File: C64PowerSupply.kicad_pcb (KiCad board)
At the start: 2 copper layers, 127 x 76.2 mm, 32 parts, among them J1 120V IN, J2 OUT C64, J3 OUT C128, SW1 120/240V SELECT, U1 BD9E303EFJ-LBE2

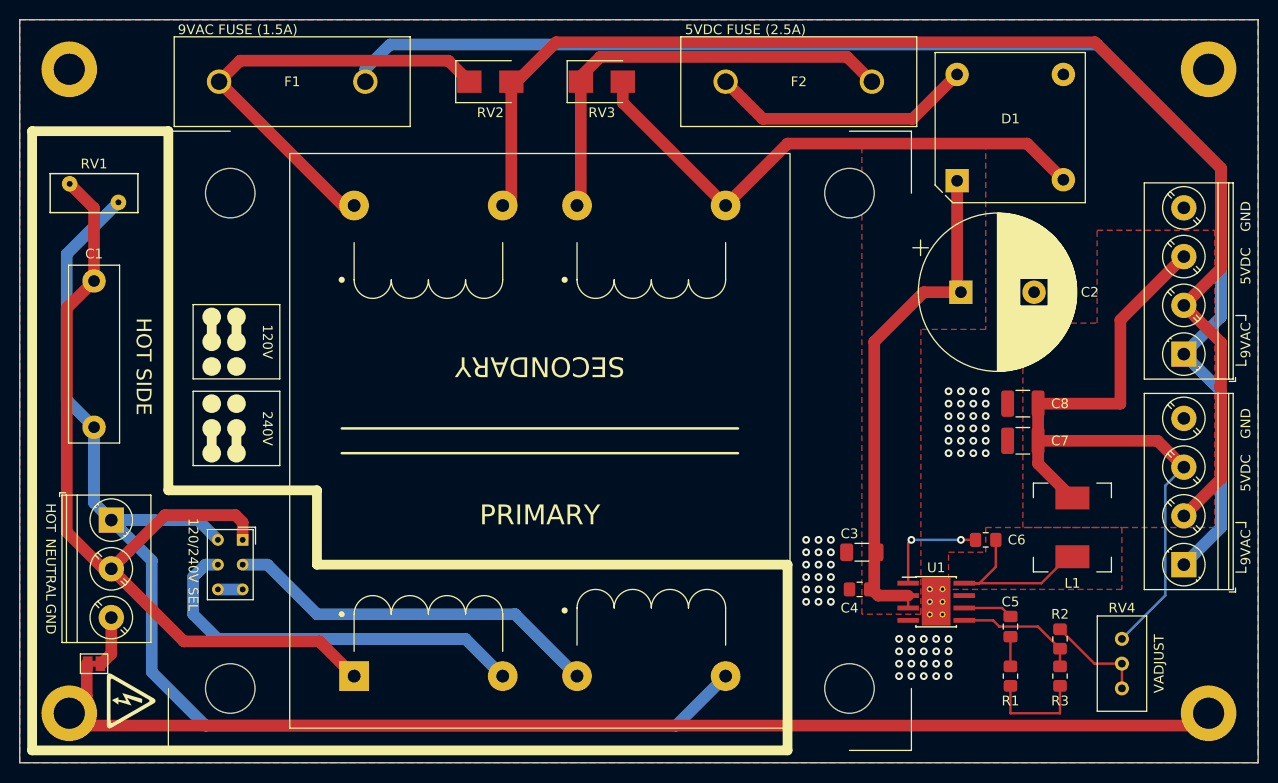
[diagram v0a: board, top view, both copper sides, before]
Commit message: Transformer hole size
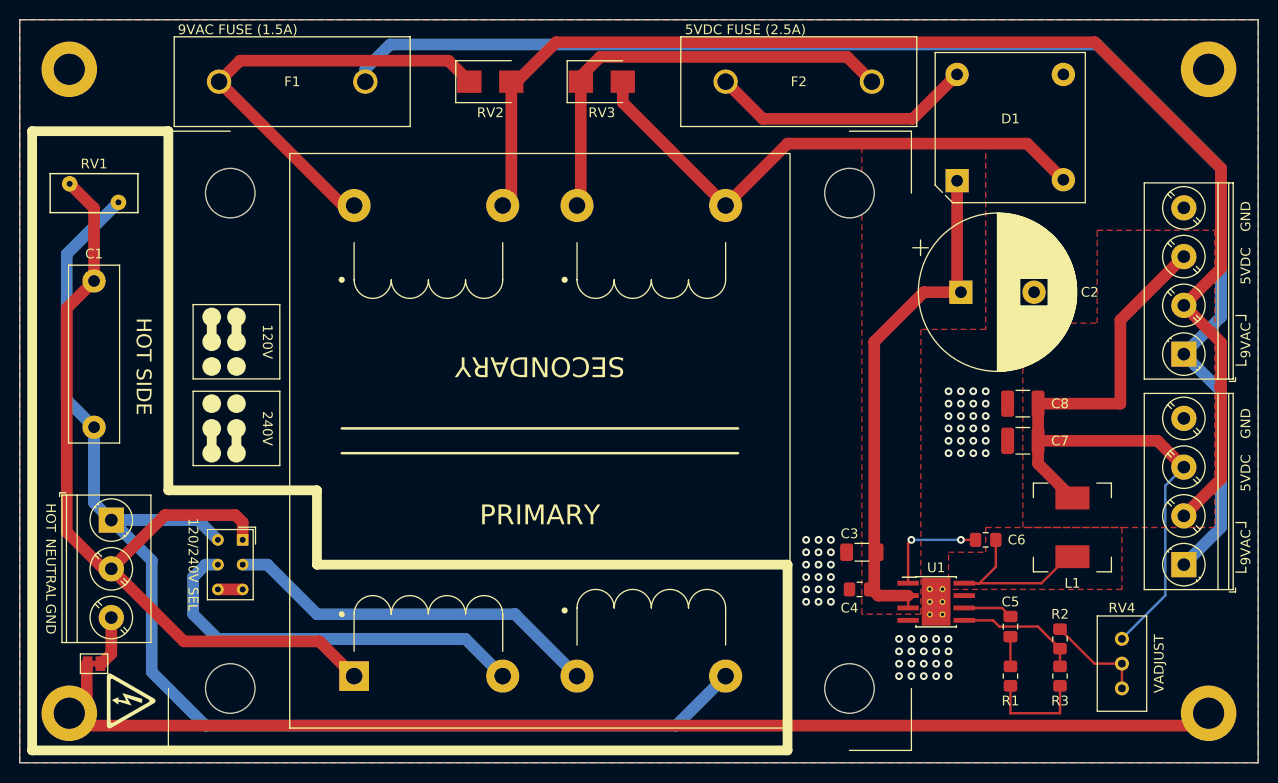
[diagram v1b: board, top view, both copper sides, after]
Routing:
- net GND: track 134.4 -> 130.8 mm

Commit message: Voltage sel switch footprint
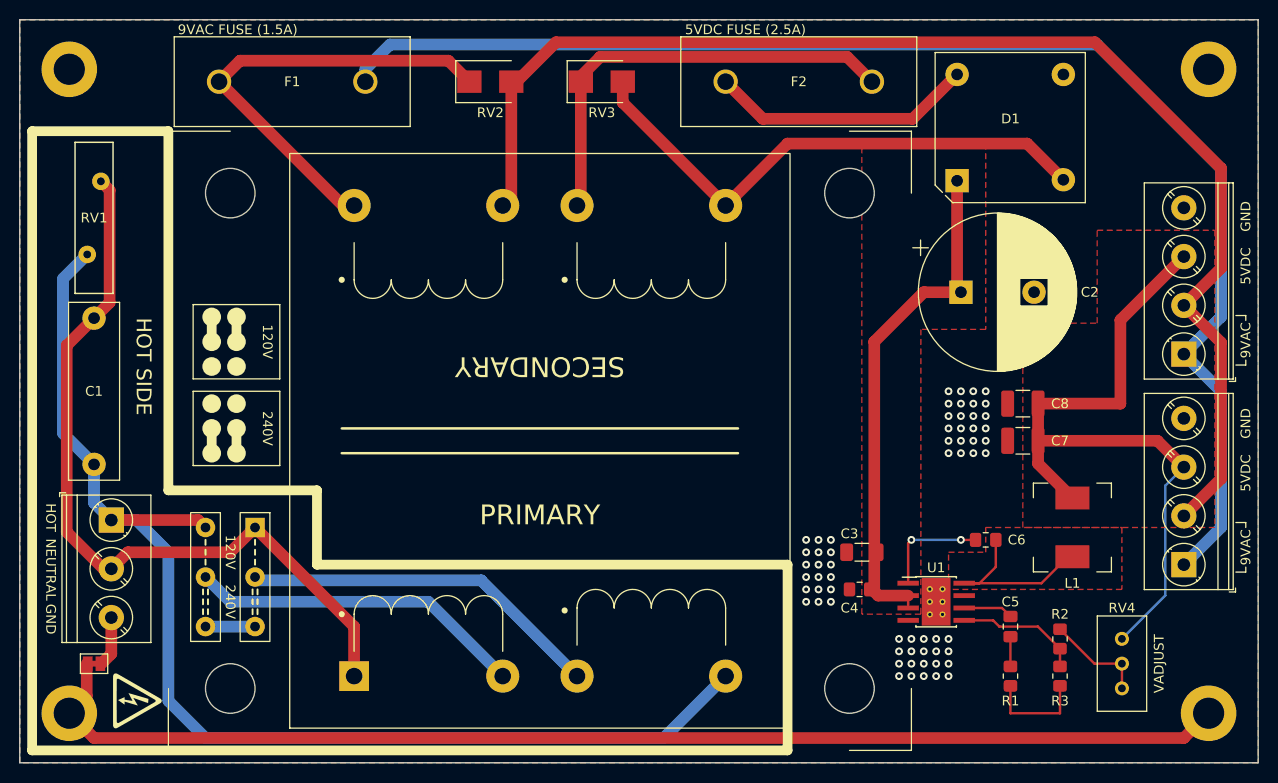
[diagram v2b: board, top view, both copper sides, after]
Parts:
- RV1: footprint Varistor:RV_Disc_D9mm_W4mm_P5mm -> Varistor:RV_Disc_D15.5mm_W3.9mm_P7.5mm
- SW1: footprint Button_Switch_THT:SW_NKK_GW12LJP -> DTLib:V_SEL_SWITCH
- moved G*** 10.2 mm to (142.2, 111.8)
- moved RV1 6.23 mm to (75.5, 74.9), turned to 90 degrees
- moved C1 3.81 mm to (76.2, 96.4)
- moved SW1 1.80 mm to (92.7, 102.9)
- moved G*** 0.63 mm to (80.6, 120.7)
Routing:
- net AC_NEUTRAL: track 91.4 -> 80.2 mm
- net Net-(SW1-Pad5): track 41.3 -> 34.7 mm
- net AC_HOT: track 129.0 -> 124.1 mm
- net Net-(SW1-Pad3): track 2.54 -> 5.08 mm
- net Net-(SW1-Pad2): track 39.0 -> 37.2 mm
- net GND: track 130.8 -> 131.9 mm
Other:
- board text removed: "120/240V SEL"

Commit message: Move cap, add logo
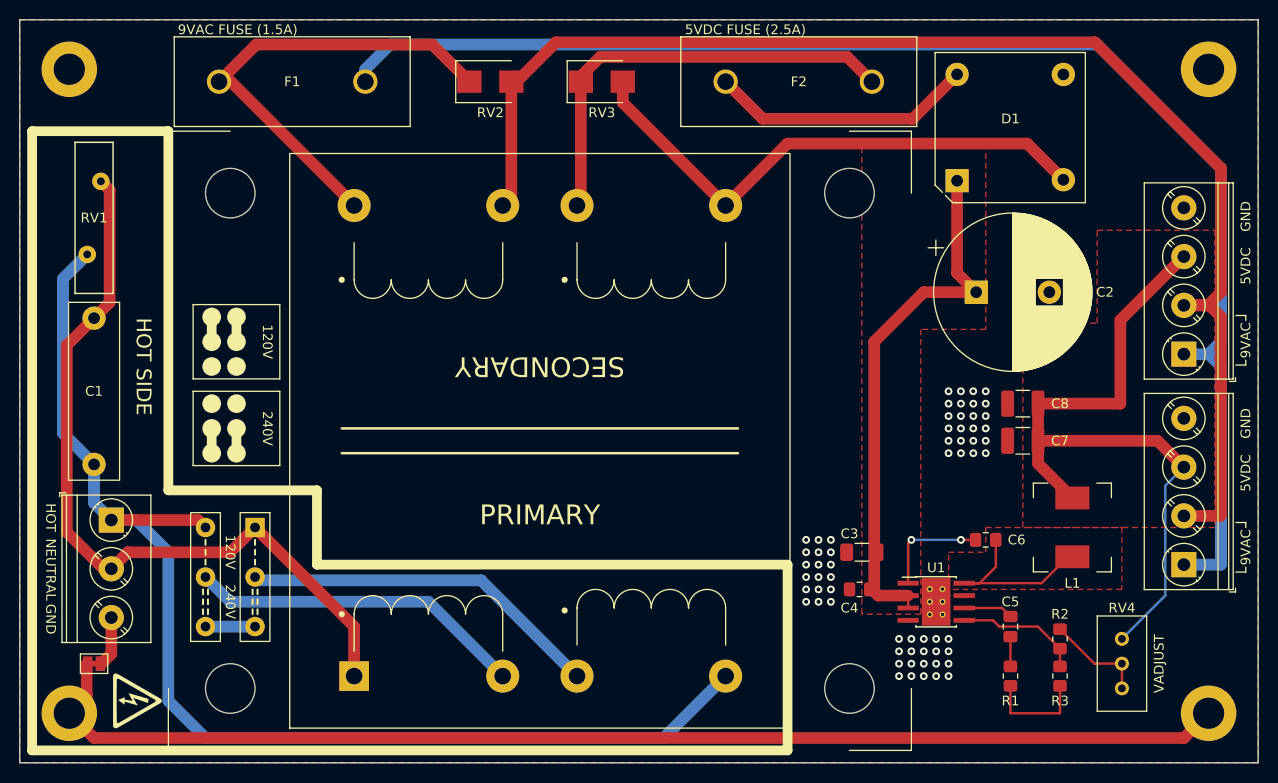
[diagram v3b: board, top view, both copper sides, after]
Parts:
- added G***: LOGO, DTLib:Logo, B.Cu at (142.2, 102.9)
- moved C2 1.57 mm to (166.7, 78.7)
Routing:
- net 9VAC_B: track 132.7 -> 137.9 mm
- net /VUNREG: track 52.6 -> 55.3 mm
- net 9VAC_A: track 140.7 -> 143.4 mm
- net Net-(F1-Pad2): track 46.6 -> 48.0 mm
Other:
- board text added: "C64/C128 Power Supply RevB 2022 Dominic Thibodeau / dev@hotkeysoft.net github.com/hotkeysoft/c64PowerSupply-kicad"
- board text removed: "C64/C128 Power Supply RevB 2022 Dominic Thibodeau https://github.com/hotkeysoft/c64PowerSupply-kicad dev@hotkeysoft.net"

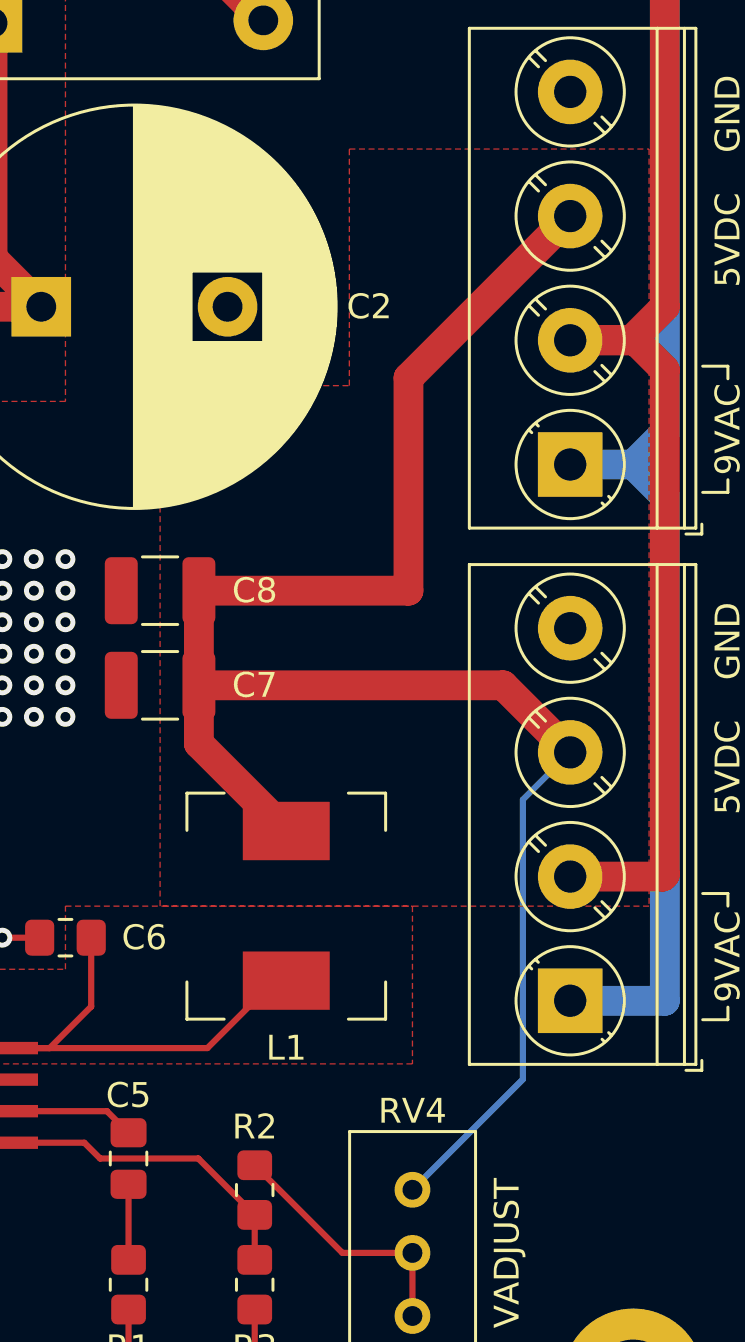
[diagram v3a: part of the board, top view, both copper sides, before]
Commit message: Plot, images, README, Fix ground plane
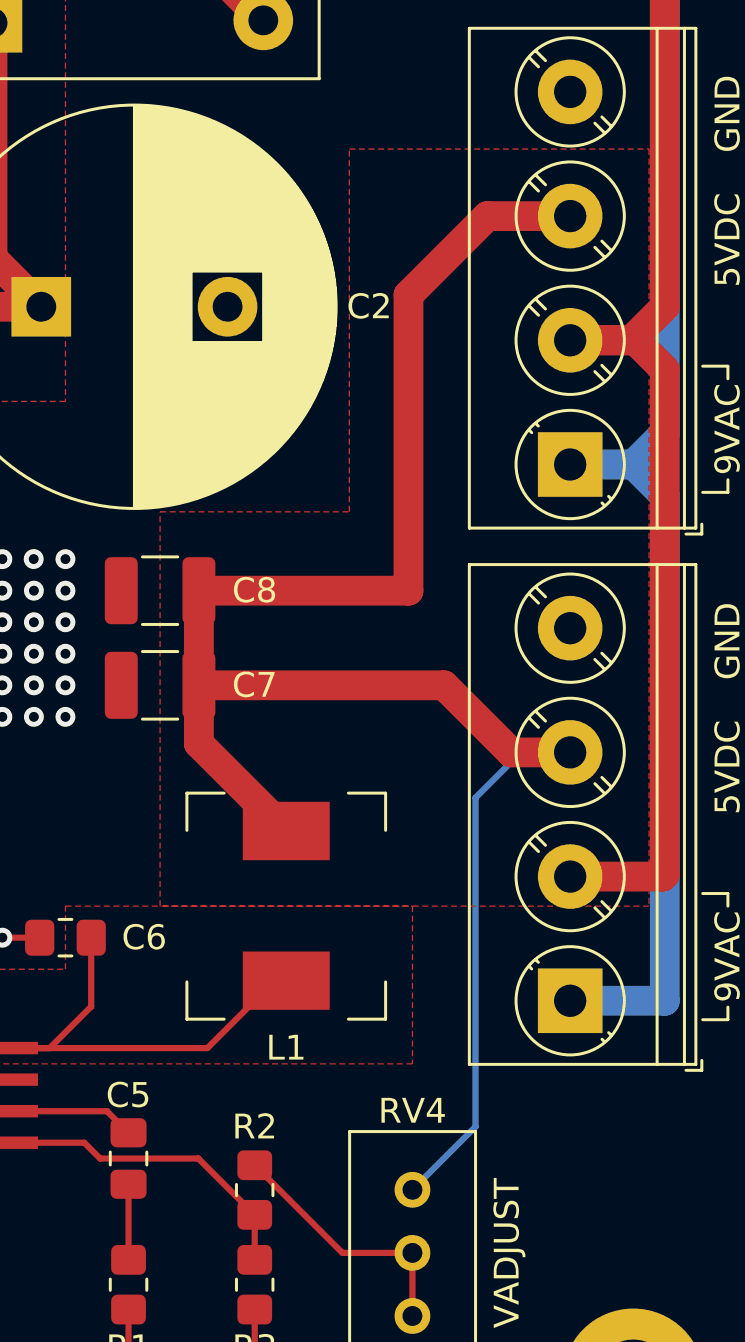
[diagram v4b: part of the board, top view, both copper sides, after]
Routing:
- net 5VDC: track 73.7 -> 76.8 mm
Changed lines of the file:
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@@
   (segment (start 173.355 108.585) (end 165.435 108.585) (width 0.25) (layer "F.Cu") (net 10))
   (segment (start 173.0125 90.17) (end 173.0125 93.98) (width 1.2) (layer "F.Cu") (net 11))
-  (segment (start 173.0125 90.17) (end 181.45 90.17) (width 1.2) (layer "F.Cu") (net 11))
-  (segment (start 187.96 75.09) (end 181.45 81.6) (width 1.2) (layer "F.Cu") (net 11))
-  (segment (start 173.0125 93.98) (end 185.26 93.98) (width 1.2) (layer "F.Cu") (net 11))
-  (segment (start 181.45 81.6) (end 181.45 90.17) (width 1.2) (layer "F.Cu") (net 11))
+  (segment (start 187.96 75.09) (end 184.625 75.09) (width 1.2) (layer "F.Cu") (net 11))
+  (segment (start 181.45 78.265) (end 181.45 90.17) (width 1.2) (layer "F.Cu") (net 11))
   (segment (start 173.0125 93.98) (end 173.0125 96.3275) (width 1.2) (layer "F.Cu") (net 11))
+  (segment (start 182.88 93.98) (end 185.58 96.68) (width 1.2) (layer "F.Cu") (net 11))
+  (segment (start 185.58 96.68) (end 187.96 96.68) (width 1.2) (layer "F.Cu") (net 11))
   (segment (start 173.0125 96.3275) (end 176.53 99.845) (width 1.2) (layer "F.Cu") (net 11))
-  (segment (start 185.26 93.98) (end 187.96 96.68) (width 1.2) (layer "F.Cu") (net 11))
-  (segment (start 181.61 114.29) (end 186.055 109.845) (width 0.25) (layer "B.Cu") (net 11))
-  (segment (start 186.055 98.585) (end 187.96 96.68) (width 0.25) (layer "B.Cu") (net 11))
-  (segment (start 186.055 109.845) (end 186.055 98.585) (width 0.25) (layer "B.Cu") (net 11))
+  (segment (start 184.625 75.09) (end 181.45 78.265) (width 1.2) (layer "F.Cu") (net 11))
+  (segment (start 173.0125 93.98) (end 182.88 93.98) (width 1.2) (layer "F.Cu") (net 11))
+  (segment (start 181.45 90.17) (end 173.0125 90.17) (width 1.2) (layer "F.Cu") (net 11))
+  (segment (start 184.15 98.505) (end 185.975 96.68) (width 0.25) (layer "B.Cu") (net 11))
+  (segment (start 185.975 96.68) (end 187.96 96.68) (width 0.25) (layer "B.Cu") (net 11))
+  (segment (start 184.15 111.75) (end 184.15 98.505) (width 0.25) (layer "B.Cu") (net 11))
+  (segment (start 181.61 114.29) (end 184.15 111.75) (width 0.25) (layer "B.Cu") (net 11))
   (segment (start 175.26 115.3) (end 172.99 113.03) (width 0.25) (layer "F.Cu") (net 12))
   (segment (start 175.26 115.3) (end 175.26 117.11) (width 0.25) (layer "F.Cu") (net 12))
@@
         (xy 191.135 102.87)
         (xy 171.45 102.87)
-        (xy 171.45 81.915)
-        (xy 179.07 81.915)
+        (xy 171.45 86.995)
+        (xy 179.07 86.995)
         (xy 179.07 72.39)
         (xy 191.135 72.39)
@@
     (connect_pads thru_hole_only (clearance 0.508))
     (min_thickness 0.254) (filled_areas_thickness no)
-    (fill yes (thermal_gap 0.508) (thermal_bridge_width 1))
+    (fill yes (thermal_gap 0.508) (thermal_bridge_width 1) (smoothing fillet) (radius 0.254))
     (polygon
       (pts
@@
     (polygon
       (pts
-        (xy 185.42 109.22)
-        (xy 171.45 109.22)
-        (xy 171.45 83.82)
-        (xy 185.42 83.82)
+        (xy 182.245 109.22)
+        (xy 170.815 109.22)
+        (xy 170.815 95.885)
+        (xy 182.245 95.885)
       )
     )

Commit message: Bumped C2 to 2200uF
1000uF worked fine @ 2A but regulation dropped quickly after
because ripple was too large. 2200uF is enough to go up to 3A.
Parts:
- C2: value 1000μF -> 2200μF
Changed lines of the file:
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@@
       (effects (font (size 1 1) (thickness 0.15)))
     )
-    (fp_text value "1000μF" (at 3.75 9.25) (layer "F.Fab")
+    (fp_text value "2200μF" (at 3.75 9.25) (layer "F.Fab")
       (effects (font (size 1 1) (thickness 0.15)))
     )
